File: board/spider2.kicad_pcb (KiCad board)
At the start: 2 copper layers, 137 x 75.5 mm, 127 parts, among them J1 NRJ6HH-1, J10 PJ-320A, J11 PJ358, J12 PJ358, J13 PJ358, J14 PJ358, J15 PJ358, J16 PJ359, J19 PJ358, J2 NRJ6HH-1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

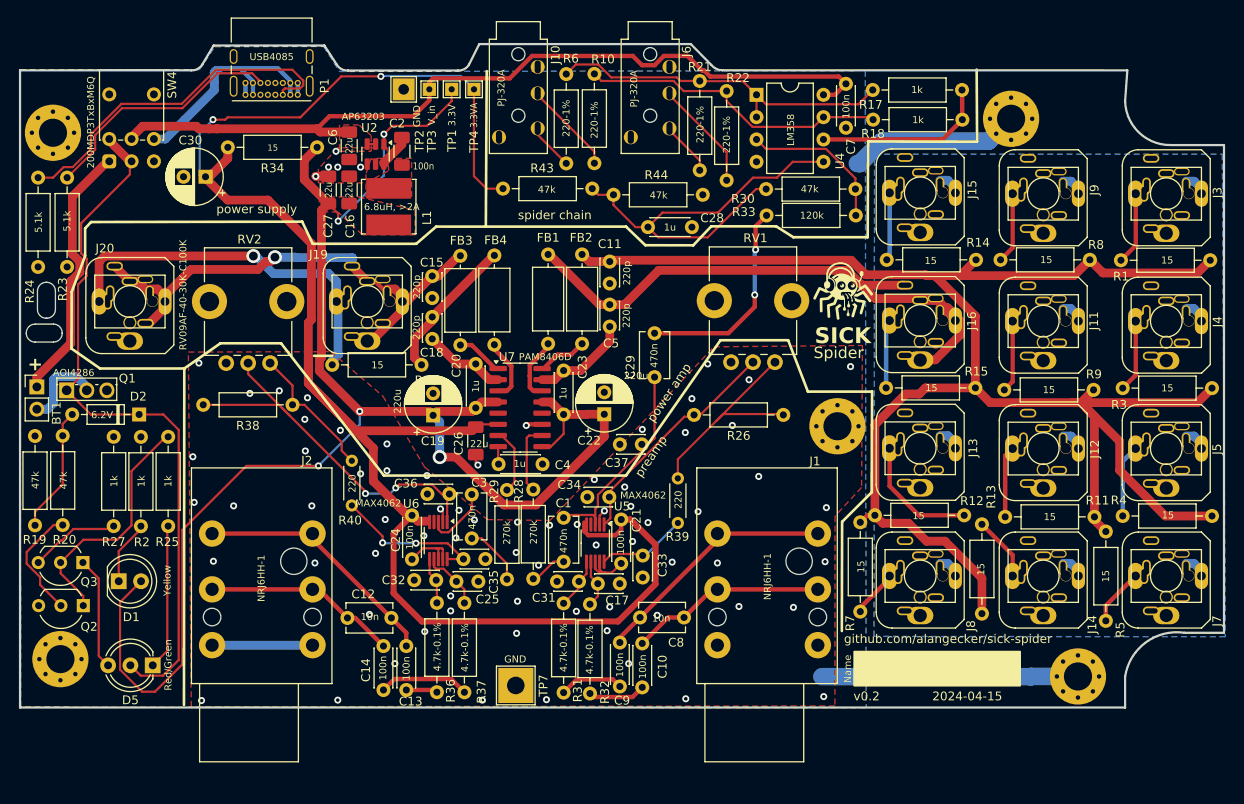
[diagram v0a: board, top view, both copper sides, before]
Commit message: minor changes (silkscreen, etc.)
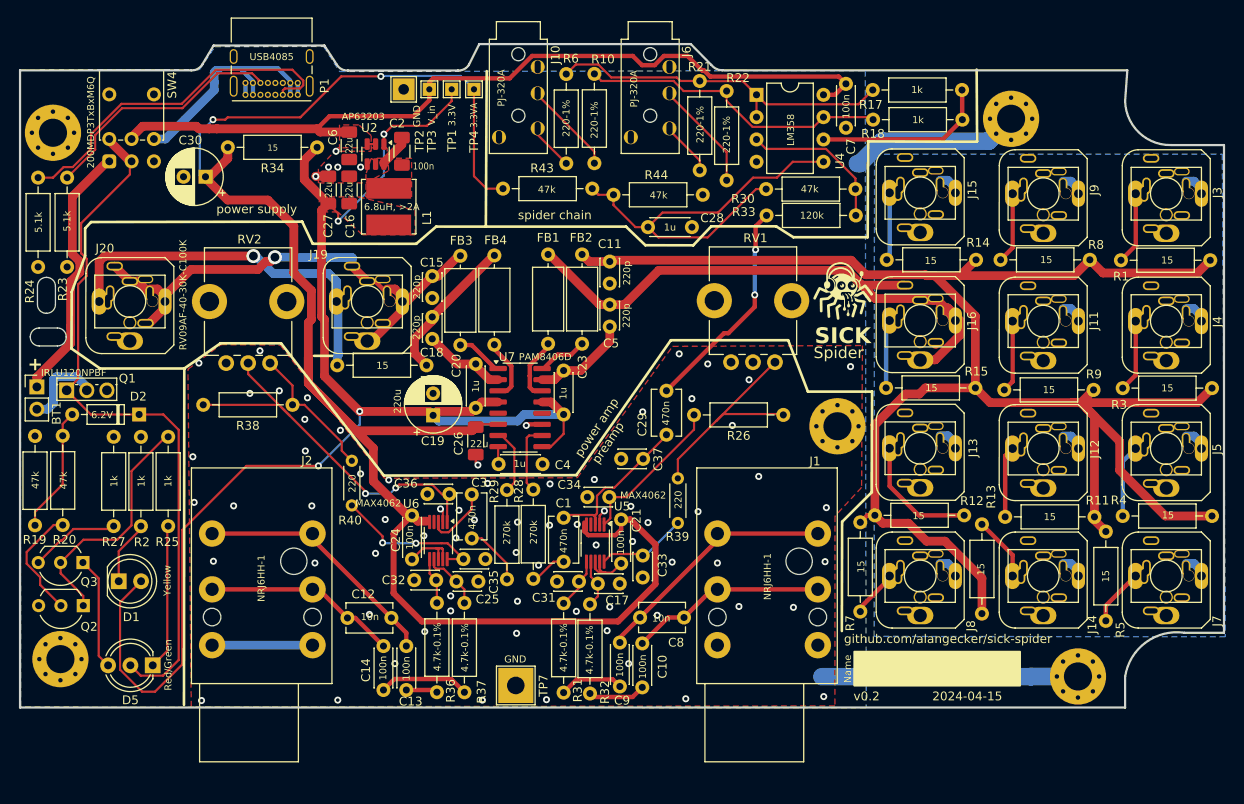
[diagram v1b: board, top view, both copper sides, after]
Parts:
- removed C22: 220u, Capacitor_THT:CP_Radial_D6.3mm_P2.50mm
- Q1: value AOI4286 -> IRLU120NPBF
- moved C29 6.69 mm to (211.2, 67.0)
- moved C37 1.66 mm to (206.1, 74.8)
- moved R16 0.57 mm to (183.9, 64.2)
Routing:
- net +3.3V: track 184.2 -> 163.0 mm, vias 5 -> 4
- net Net-(U5-G2): track 26.9 -> 18.3 mm
- net INT_OUT: track 24.2 -> 18.9 mm
- net Net-(C29-Pad1): track 23.6 -> 25.0 mm
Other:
- outline, holes or cut-outs redrawn

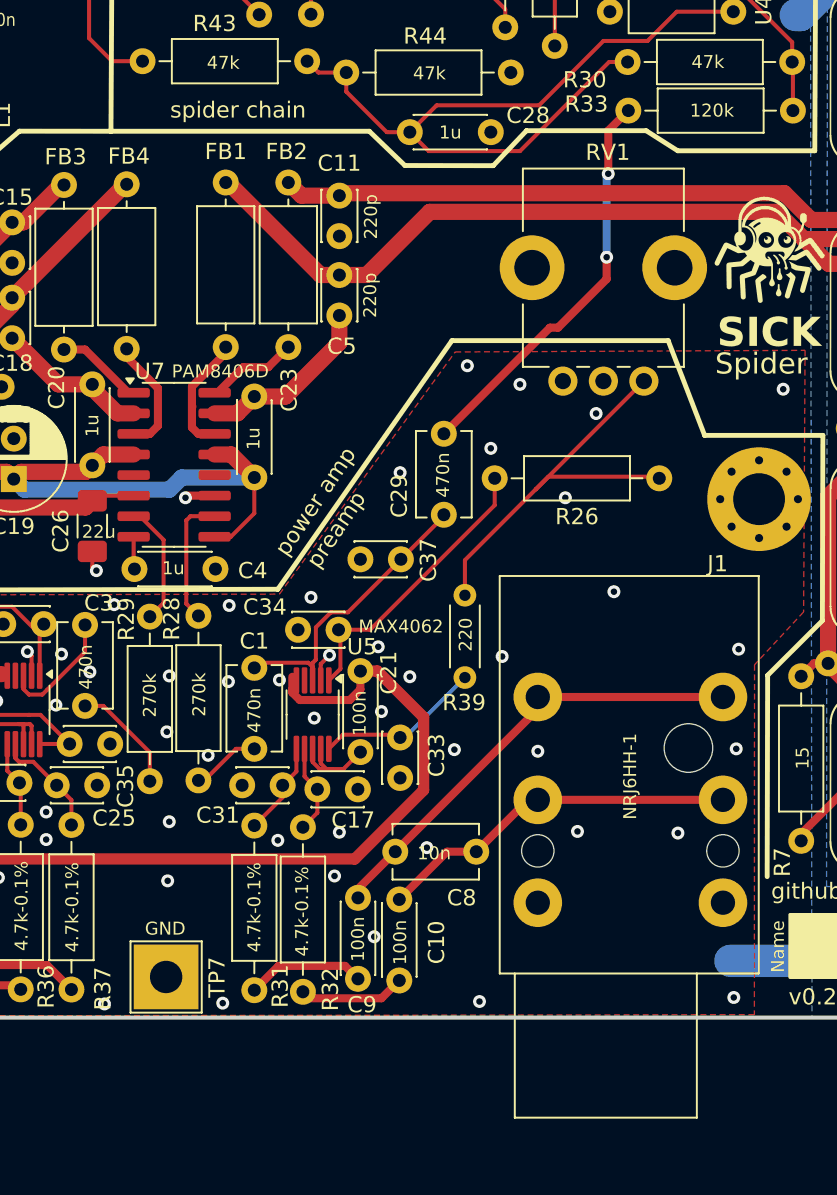
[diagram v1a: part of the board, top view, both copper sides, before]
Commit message: add some spare capacitors for EMI tests
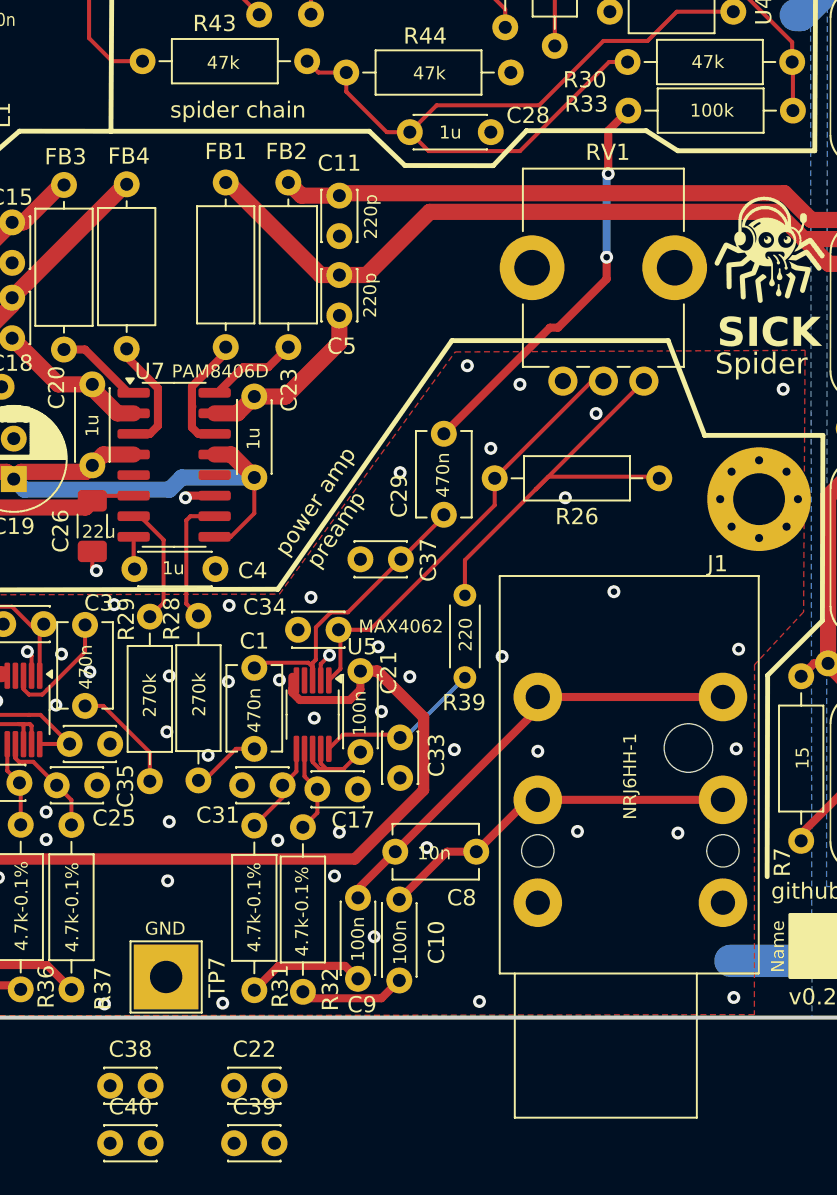
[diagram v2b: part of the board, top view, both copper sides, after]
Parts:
- added C22: 220p, Capacitor_THT:C_Disc_D3.0mm_W2.0mm_P2.50mm, F.Cu at (198.2, 107.3)
- added C38: 220p, Capacitor_THT:C_Disc_D3.0mm_W2.0mm_P2.50mm, F.Cu at (190.6, 107.3)
- added C39: 220p, Capacitor_THT:C_Disc_D3.0mm_W2.0mm_P2.50mm, F.Cu at (198.2, 110.8)
- added C40: 220p, Capacitor_THT:C_Disc_D3.0mm_W2.0mm_P2.50mm, F.Cu at (190.6, 110.8)
- R33: value 120k -> 100k
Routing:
- net Net-(U5-G2): track 18.3 -> 27.5 mm

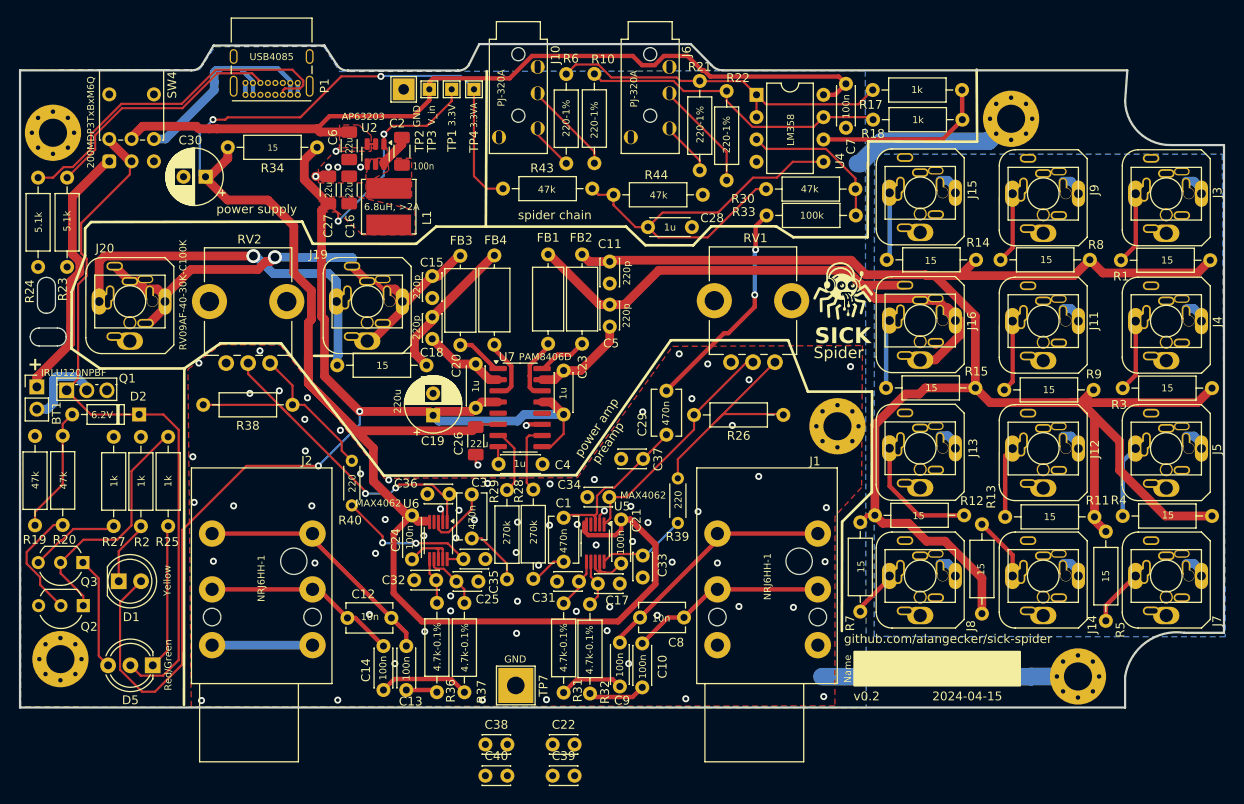
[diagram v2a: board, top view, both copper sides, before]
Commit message: more EMI protection C's and poti inverting jumper
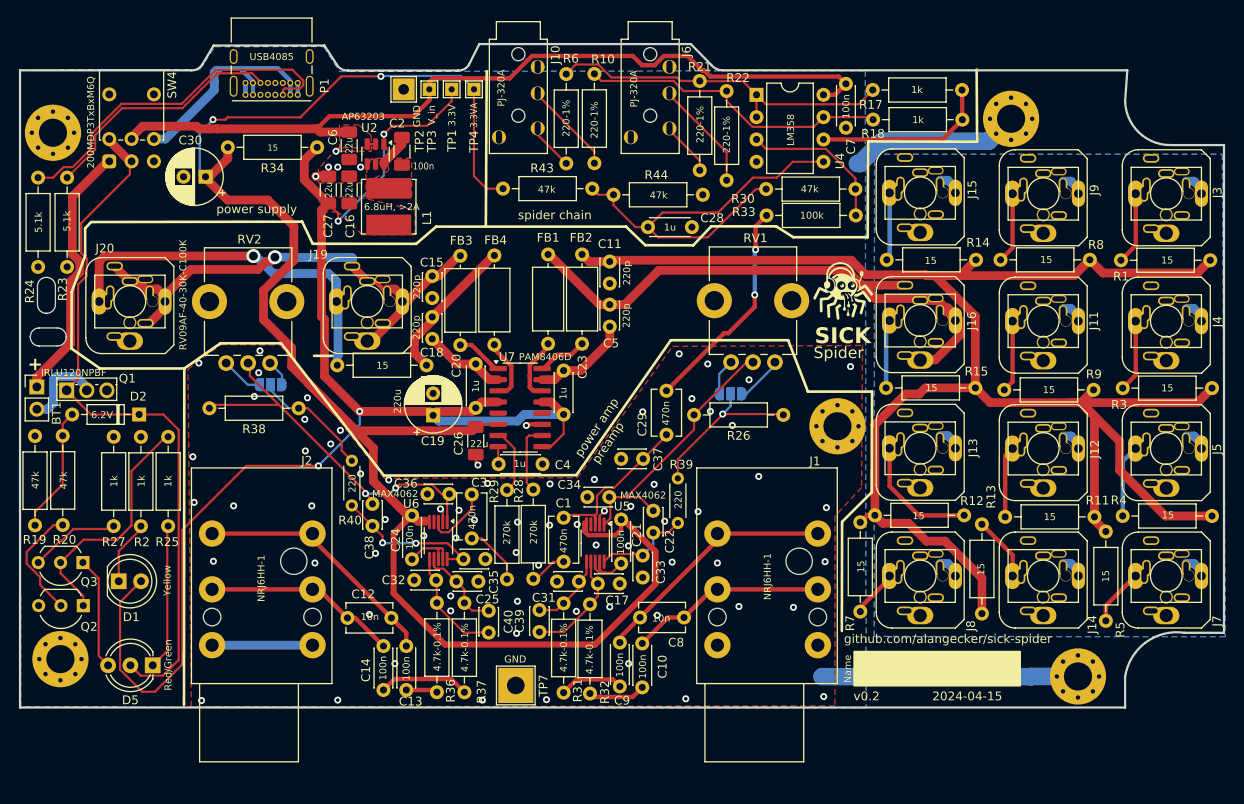
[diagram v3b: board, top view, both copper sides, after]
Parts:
- added JP1: ~, Jumper:SolderJumper-3_P1.3mm_Open_RoundedPad1.0x1.5mm_NumberLabels, B.Cu at (218.5, 67.4)
- added JP2: ~, Jumper:SolderJumper-3_P1.3mm_Open_RoundedPad1.0x1.5mm_NumberLabels, B.Cu at (166.2, 66.4)
- moved C38 30.2 mm to (177.8, 79.9), turned to -90 degrees
- moved C22 29.0 mm to (209.7, 80.7), turned to -90 degrees
- moved C40 18.8 mm to (191.0, 92.1), turned to -90 degrees
- moved C39 16.4 mm to (196.8, 94.5), turned to 90 degrees
- moved R38 0.80 mm to (169.3, 69.0)
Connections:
- R26 pad 1: Net-(R26-Pad1) -> Net-(JP1-C)
- R38 pad 1: Net-(R38-Pad1) -> Net-(JP2-C)
- R39 pad 2: Net-(R26-Pad1) -> Net-(JP1-C)
- R40 pad 2: Net-(R38-Pad1) -> Net-(JP2-C)
- RV1 pad 1: Net-(R26-Pad1) -> Net-(JP1-A)
- RV1 pad 3: unconnected-(RV1-Pad3) -> Net-(JP1-B)
- RV2 pad 1: Net-(R38-Pad1) -> Net-(JP2-A)
- RV2 pad 3: unconnected-(RV2-Pad3) -> Net-(JP2-B)
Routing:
- net Net-(R26-Pad1): track 25.8 -> 0.00 mm
- net Net-(JP1-C): track 0.00 -> 19.0 mm, vias 0 -> 1
- net Net-(R38-Pad1): track 15.8 -> 0.00 mm
- net Net-(JP2-C): track 0.00 -> 13.8 mm
- net Net-(U6-IN+): track 5.32 -> 12.8 mm
- net Net-(U5-IN-): track 5.54 -> 12.7 mm
- net Net-(JP1-A): track 0.00 -> 5.45 mm
- net Net-(JP2-B): track 0.00 -> 4.78 mm
- net Net-(JP1-B): track 0.00 -> 4.16 mm
- net Net-(U5-G2): track 27.5 -> 31.2 mm
- net Net-(U6-IN-): track 6.94 -> 10.1 mm
- net Net-(U5-IN+): track 5.82 -> 8.88 mm
- net Net-(JP2-A): track 0.00 -> 3.02 mm
- net +3.3VA: track 198.2 -> 199.6 mm
- net Net-(U5-G1): track 10.4 -> 11.5 mm
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
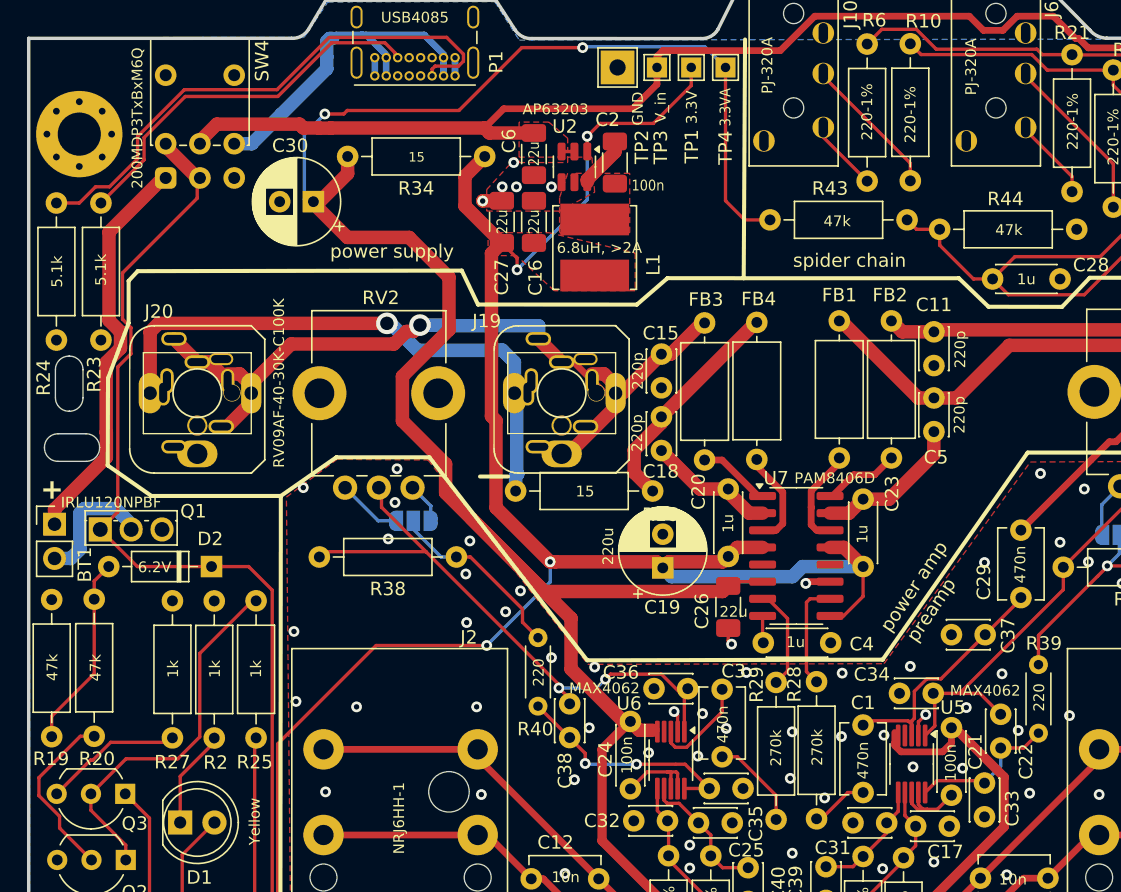
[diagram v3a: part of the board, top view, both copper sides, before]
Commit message: last changes for 0.2 (testpoints, spare footprints,...)
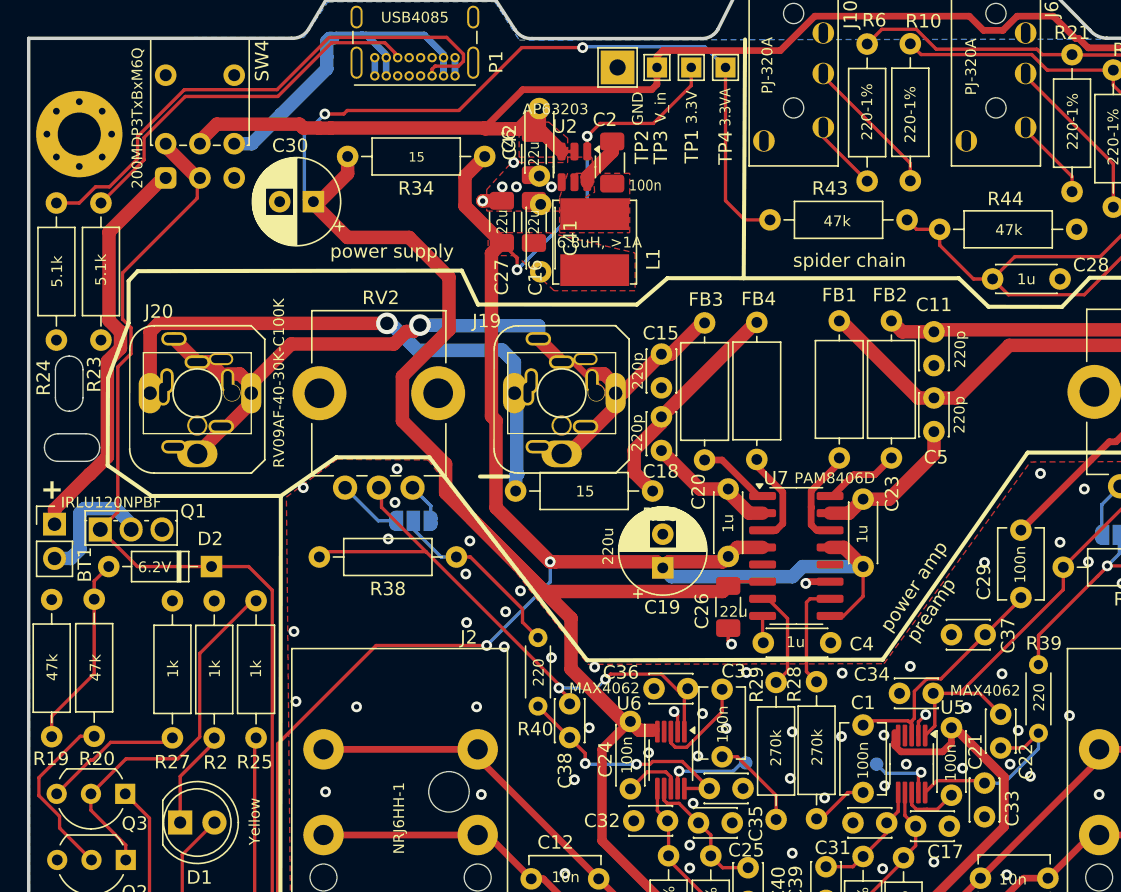
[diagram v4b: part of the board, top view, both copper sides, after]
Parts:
- added C41: dnp, Capacitor_THT:C_Disc_D4.3mm_W1.9mm_P5.00mm, F.Cu at (175.6, 42.9)
- added C42: dnp, Capacitor_THT:C_Disc_D4.3mm_W1.9mm_P5.00mm, F.Cu at (175.5, 40.8)
- added TP5: AUX_IN, TestPoint:TestPoint_Pad_D1.0mm, B.Cu at (200.5, 84.4)
- added TP6: AUX_IN, TestPoint:TestPoint_Pad_D1.0mm, B.Cu at (190.8, 84.3)
- C1, C29, C3: value 470n -> 100n
- L1: value 6.8uH, >2A -> 6.8uH, >1A
- moved L1 0.40 mm to (179.6, 45.7)
- moved C2 0.20 mm to (180.9, 39.8)
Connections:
- U5 pad 9: GND -> Net-(U5-AUX_IN)
- U6 pad 9: GND -> Net-(U6-AUX_IN)
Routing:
- net VCC: track 96.9 -> 103.8 mm
- net Net-(U6-AUX_IN): track 0.00 -> 6.67 mm, vias 0 -> 1
- net Net-(U5-AUX_IN): track 0.00 -> 5.19 mm, vias 0 -> 1
- net GND: track 104.4 -> 100.9 mm, vias 77 -> 81
- net Net-(U5-G1): track 11.5 -> 14.3 mm
- net Net-(C15-Pad2): track 61.6 -> 64.4 mm

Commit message: 0.2-prototype
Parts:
- C1, C29, C3: footprint Capacitor_THT:C_Disc_D5.1mm_W3.2mm_P5.00mm -> Capacitor_THT:C_Disc_D4.3mm_W1.9mm_P5.00mm
- J16: value PJ359 -> PJ358
- R28, R29: footprint Resistor_THT:R_Axial_DIN0207_L6.3mm_D2.5mm_P10.16mm_Horizontal -> Resistor_THT:R_Axial_DIN0207_L6.3mm_D2.5mm_P7.62mm_Horizontal
- R39, R40: value 220 -> 220-1%
- moved R29 2.84 mm to (193.1, 85.7)
- moved R28 2.80 mm to (196.2, 85.7)
- moved C1 0.65 mm to (200.2, 81.5)
- moved C3 0.55 mm to (188.5, 78.8)
- moved C36 0.25 mm to (186.2, 78.8)
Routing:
- net Net-(C3-Pad2): track 6.97 -> 5.34 mm
- net INT_OUT: track 18.9 -> 18.2 mm
- net GND: vias 81 -> 80
